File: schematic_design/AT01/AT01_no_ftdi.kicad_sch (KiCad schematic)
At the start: 69 parts, among them J1 JST Connector, J2 USB_C_Receptacle_USB2.0, J3 Conn_01x08, J4 Solenoid Valve Connector, J5 DC Pump Connector, J6 PPG Sensor Input, K1 TLP4590ATP1_F, Q2 FDS6375, SW1 SW_Push, SW2 SW_Push, SW3 SW_Push, SW4 SW_Push, U1 MPRLS0025PA00001A, U2 LT1935ES5-TRPBF, U3 MCP73844T-840I/MS, U4 LM1117T-3.3, U5 DRV8833PW, U6 ESP32-S3-WROOM

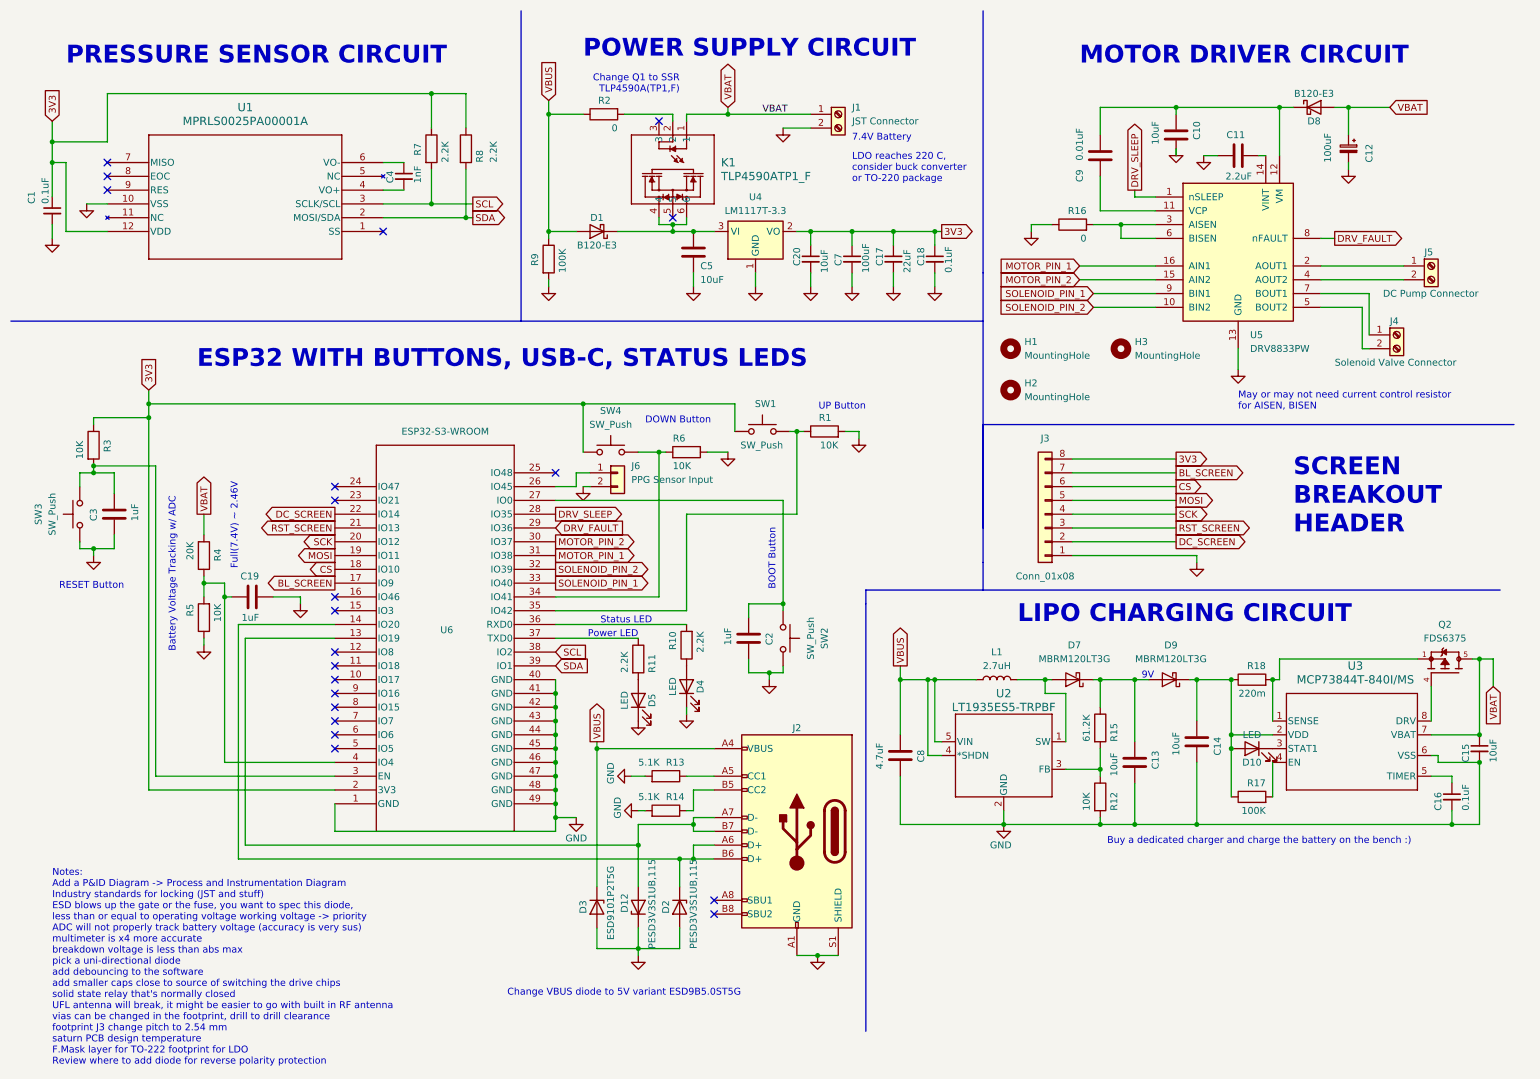
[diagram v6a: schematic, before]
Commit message: reworking usb c connection
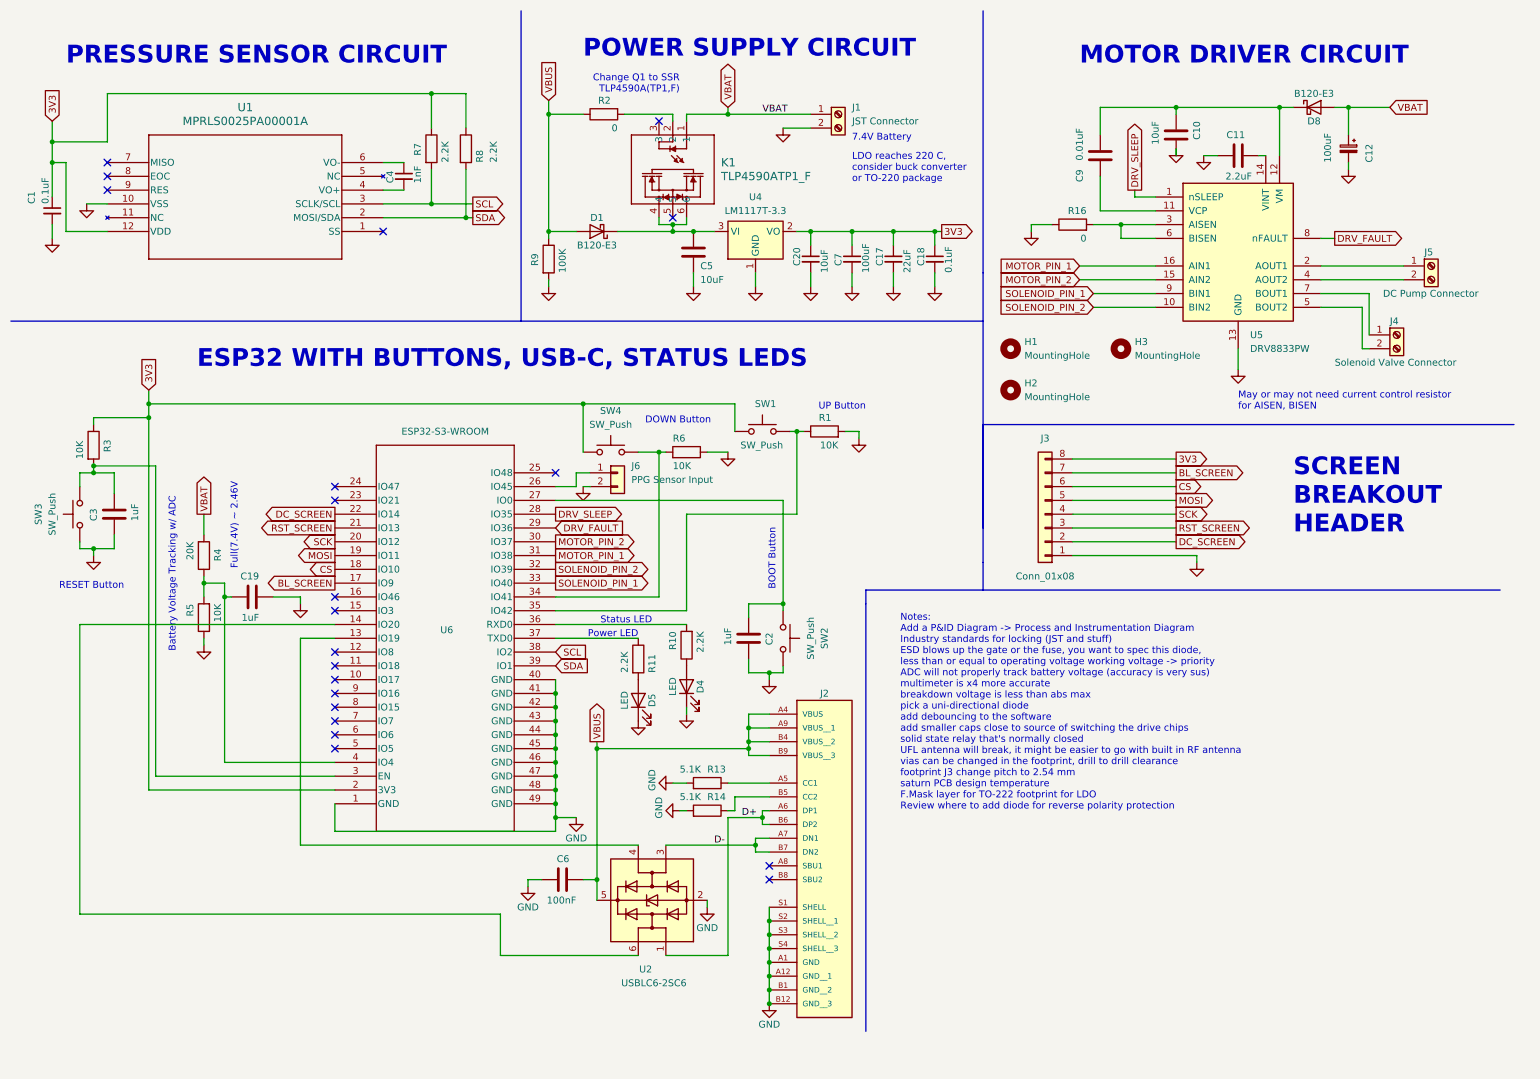
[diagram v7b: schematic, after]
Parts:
- removed C13, C14: 10uF, Capacitor_SMD:C_0603_1608Metric_Pad1.08x0.95mm_HandSolder, symbol Device:C
- removed C15: 10uF, Capacitor_SMD:C_0603_1608Metric_Pad1.08x0.95mm_HandSolder, symbol Device:C_Small
- removed C16: 0.1uF, Capacitor_SMD:C_0603_1608Metric_Pad1.08x0.95mm_HandSolder, symbol Device:C_Small
- removed C8: 4.7uF, Capacitor_SMD:C_0603_1608Metric_Pad1.08x0.95mm_HandSolder, symbol Device:C
- removed D10: LED, LED_THT:LED_D3.0mm, symbol Device:LED
- removed D12, D2: PESD3V3S1UB,115, Diode_SMD:D_SOD-523, symbol Device:D_Zener
- removed D3: ESD9101P2T5G, Diode_SMD:D_SOD-923, symbol Device:D_Zener
- removed D7, D9: MBRM120LT3G, Diode_SMD:D_SOD-123F, symbol Diode:MBR1020VL
- removed L1: 2.7uH, Library:IND_R2NC_SUM, symbol Device:L
- removed Q2: FDS6375, Library:SOIC127P600X175-8N, symbol FDS6375:FDS6375
- removed R12: 10K, Resistor_SMD:R_0603_1608Metric_Pad0.98x0.95mm_HandSolder, symbol Device:R
- removed R15: 61.2K, Resistor_SMD:R_0402_1005Metric_Pad0.72x0.64mm_HandSolder, symbol Device:R
- removed R17: 100K, Resistor_SMD:R_0603_1608Metric_Pad0.98x0.95mm_HandSolder, symbol Device:R
- removed R18: 220m, Resistor_SMD:R_0603_1608Metric_Pad0.98x0.95mm_HandSolder, symbol Device:R
- removed U2: LT1935ES5-TRPBF, S_5_ADI, symbol 2023-10-27_15-39-09:LT1935ES5-TRPBF
- removed U3: MCP73844T-840I/MS, MSOP8_MC_MCH, symbol 2023-10-27_15-39-09:MCP73844T-840I_MS
- added C6: 100nF, Capacitor_SMD:C_0603_1608Metric_Pad1.08x0.95mm_HandSolder, symbol Device:C
- added U2: USBLC6-2SC6, Package_TO_SOT_SMD:SOT-23-6, symbol Power_Protection:USBLC6-2SC6
- J2: footprint Connector_USB:USB_C_Receptacle_HRO_TYPE-C-31-M-12 -> Library:GCT_USB4085-GF-A_REVB; symbol Connector:USB_C_Receptacle_USB2.0 -> 2023-10-27_15-39-09:USB4085-GF-A_REVB; MANUFACTURER (none) -> Global Connector Technology; MAXIMUM_PACKAGE_HEIGHT (none) -> 3.16mm; PARTREV (none) -> B; SNAPEDA_PN (none) -> USB4085-GF-A; STANDARD (none) -> Manufacturer Recommendations
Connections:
- net GND: now also J2.S2 (SHELL__1), J2.S3 (SHELL__2), J2.S4 (SHELL__3), C6.1, U2.2 (GND)
- net VBUS: now also C6.2, U2.5 (VBUS)
- net D-: now reaches J2.A7 (DN1), J2.B7 (DN2)
- net D-: now also U2.3 (I/O2); no longer U6.13 (IO19)
- net D+: now reaches J2.A6 (DP1), J2.B6 (DP2)
- net D+: now also U2.1 (I/O1); no longer U6.14 (IO20)
- new net: U2.4 (I/O2), U6.13 (IO19)
- new net: U2.6 (I/O1), U6.14 (IO20)
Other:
- note removed: "9V"
- note removed: "Buy a dedicated charger and charge the battery on the bench :)"
- note removed: "Change VBUS diode to 5V variant ESD9B5.0ST5G"
- note removed: "LIPO CHARGING CIRCUIT"
- moved on the sheet: R13, R14

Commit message: new code and some schematic work
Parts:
- removed C6: 100nF, Capacitor_SMD:C_0603_1608Metric_Pad1.08x0.95mm_HandSolder, symbol Device:C
- removed D1, D8: B120-E3, Diode_SMD:D_SMA, symbol Diode:B120-E3
- removed U2: USBLC6-2SC6, Package_TO_SOT_SMD:SOT-23-6, symbol Power_Protection:USBLC6-2SC6
- added D2: B120-E3, Diode_SMD:D_SMA, symbol Diode:B120-E3
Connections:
- net VBAT: now also C10.2, C9.2, U5.12 (VM), D2.1 (K), D2.2 (A)
- net at C5.1, K1.4, U4.3 (VI): now also K1.2; no longer K1.6
- net at R2.2: now also K1.5; no longer K1.2
- net D+: no longer names the net of J2.A6 (DP1)
- net D+: no longer J2.B6 (DP2)
- net D-: no longer names the net of J2.A7 (DN1)
- net D-: no longer J2.B7 (DN2)
- no-connect marks 21 -> 27
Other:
- moved on the sheet: C5, K1, R2, R9
